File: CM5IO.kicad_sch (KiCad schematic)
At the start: 12 parts, among them J11 USB_C_Receptacle_USB2.0

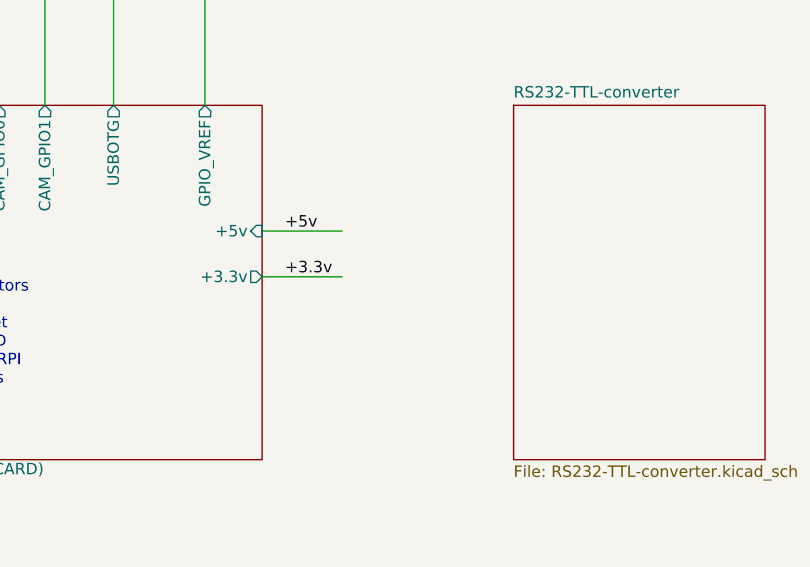
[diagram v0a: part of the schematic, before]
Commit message: Added level shifter
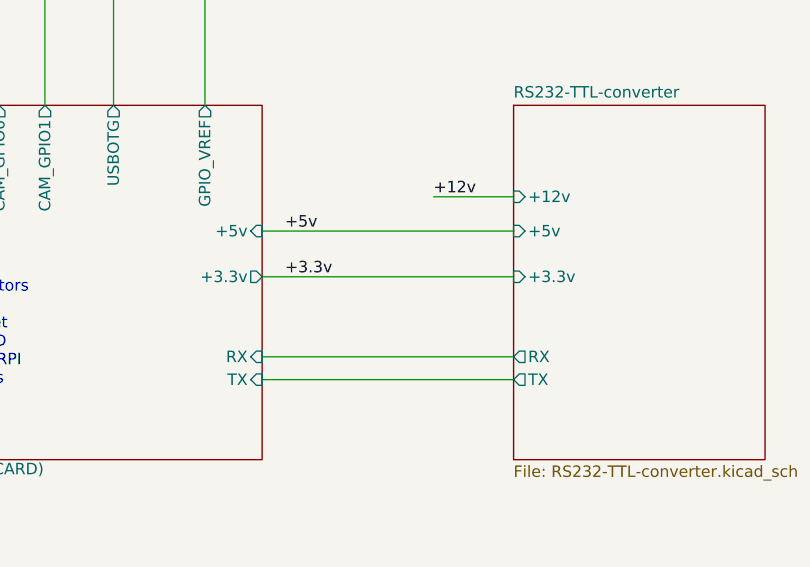
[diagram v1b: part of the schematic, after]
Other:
- sheet CM5_GPIO ( Ethernet, GPIO, SDCARD) ports: added RX, TX; removed none
- sheet RS232-TTL-converter ports: added +12v, +3.3v, +5v, RX, TX; removed none
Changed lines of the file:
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@@
 	(wire
 		(pts
-			(xy 186.69 130.81) (xy 195.58 130.81)
+			(xy 186.69 130.81) (xy 214.63 130.81)
 		)
 		(stroke
@@
 	(wire
 		(pts
+			(xy 205.74 121.92) (xy 214.63 121.92)
+		)
+		(stroke
+			(width 0)
+			(type default)
+		)
+	)
+	(wire
+		(pts
 			(xy 62.23 52.07) (xy 74.93 52.07)
 		)
@@
 	(wire
 		(pts
+			(xy 186.69 142.24) (xy 214.63 142.24)
+		)
+		(stroke
+			(width 0)
+			(type default)
+		)
+	)
+	(wire
+		(pts
 			(xy 62.23 49.53) (xy 74.93 49.53)
 		)
@@
 	(wire
 		(pts
-			(xy 186.69 125.73) (xy 195.58 125.73)
+			(xy 186.69 125.73) (xy 214.63 125.73)
+		)
+		(stroke
+			(width 0)
+			(type default)
+		)
+	)
+	(wire
+		(pts
+			(xy 186.69 139.7) (xy 214.63 139.7)
 		)
 		(stroke
@@
 	(label "CC1"
 		(at 64.77 49.53 0)
+		(effects
+			(font
+				(size 1.27 1.27)
+			)
+			(justify left bottom)
+		)
+	)
+	(label "+12v"
+		(at 205.74 121.92 0)
 		(effects
 			(font
@@
 			)
 		)
+		(pin "RX" input
+			(at 186.69 139.7 0)
+			(effects
+				(font
+					(size 1.27 1.27)
+				)
+				(justify right)
+			)
+		)
+		(pin "TX" input
+			(at 186.69 142.24 0)
+			(effects
+				(font
+					(size 1.27 1.27)
+				)
+				(justify right)
+			)
+		)
 		(instances
 			(project "CM5IO"
@@
 			)
 		)
+		(pin "+3.3v" input
+			(at 214.63 130.81 180)
+			(effects
+				(font
+					(size 1.27 1.27)
+				)
+				(justify left)
+			)
+		)
+		(pin "+5v" input
+			(at 214.63 125.73 180)
+			(effects
+				(font
+					(size 1.27 1.27)
+				)
+				(justify left)
+			)
+		)
+		(pin "+12v" input
+			(at 214.63 121.92 180)
+			(effects
+				(font
+					(size 1.27 1.27)
+				)
+				(justify left)
+			)
+		)
+		(pin "RX" output
+			(at 214.63 139.7 180)
+			(effects
+				(font
+					(size 1.27 1.27)
+				)
+				(justify left)
+			)
+		)
+		(pin "TX" output
+			(at 214.63 142.24 180)
+			(effects
+				(font
+					(size 1.27 1.27)
+				)
+				(justify left)
+			)
+		)

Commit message: Need to fix ERC
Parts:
- renumbered C9 to C1, C18 to C2, J11 to J1, R9 to R1
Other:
- removed sheet PCIe-M2
- added sheet USB-UART-converter (USB-UART-converter.kicad_sch)
- sheet CM5_GPIO ( Ethernet, GPIO, SDCARD) ports: added DeviceRX, DeviceTX; removed RX, TX
- sheet CM5_HighSpeed ports: added none; removed PCIE_CLK_N, PCIE_CLK_P, PCIE_PWR_EN, PCIE_RX_N, PCIE_RX_P, PCIE_TX_N, PCIE_TX_P, PCIE_nCLKREQ, PCIE_nRST, PCIE_nWAKE
- sheet RS232-TTL-converter ports: added DeviceRX, DeviceTX; removed +12v, +3.3v, RX, TX
- note added: "Connectors ------- CSI/DSI 0 CSI/DSI 1"
- note added: "Connectors ------- DB9"
- note added: "Connectors ------- Ethernet 40way RPI"
- note added: "Connectors ------- USB B Molex"
- note removed: "Connectors ------ M2 MKey"
- note removed: "Connectors ------- Ethernet SDCARD 40way RPI Jumpers Fan Battery"
- note removed: "Connectors ------- HDMI 0 HDMI 1 CSI/DSI 0 CSI/DSI 1"
- moved on the sheet: C1, C2, J1, R1

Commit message: schematic review
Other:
- sheet CM5_GPIO ( Ethernet, GPIO, SDCARD) ports: added RX, TX; removed DeviceRX, DeviceTX
- sheet RS232-TTL-converter ports: added RX, TX; removed none
- company: Copyright © 2024 Raspberry Pi Ltd. -> Astrosystems
- title: Compute Module 5 IO Board - Top Level -> CM4/5 UART Sniffer
- moved on the sheet: C1, C2, J1, R1

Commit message: updated files
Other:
- sheet RS232-TTL-converter ports: added +3.3v; removed none
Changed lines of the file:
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@@
+	(wire
+		(pts
+			(xy 215.9 116.84) (xy 228.6 116.84)
+		)
+		(stroke
+			(width 0)
+			(type default)
+		)
+	)
 	(wire
 		(pts
@@
 	(wire
 		(pts
-			(xy 215.9 133.35) (xy 228.6 133.35)
+			(xy 215.9 120.65) (xy 228.6 120.65)
 		)
 		(stroke
@@
 		)
 	)
+	(label "+3.3v"
+		(at 215.9 116.84 0)
+		(effects
+			(font
+				(size 1.27 1.27)
+			)
+			(justify left bottom)
+		)
+	)
 	(label "+5v"
 		(at 72.39 127 180)
@@
 		)
 	)
+	(label "+3.3v"
+		(at 154.94 87.63 0)
+		(effects
+			(font
+				(size 1.27 1.27)
+			)
+			(justify left bottom)
+		)
+	)
 	(label "+5v"
-		(at 215.9 133.35 0)
+		(at 215.9 120.65 0)
 		(effects
 			(font
@@
 		)
 		(pin "+5v" input
-			(at 228.6 133.35 180)
+			(at 228.6 120.65 180)
 			(effects
 				(font
@@
 			)
 		)
+		(pin "+3.3v" input
+			(at 228.6 116.84 180)
+			(effects
+				(font
+					(size 1.27 1.27)
+				)
+				(justify left)
+			)
+		)
